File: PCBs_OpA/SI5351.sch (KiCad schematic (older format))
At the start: 12 parts, among them J4 CAL, Q1 2N7002, Q2 2N7002, U2 Si5351, Y1 25Mhz

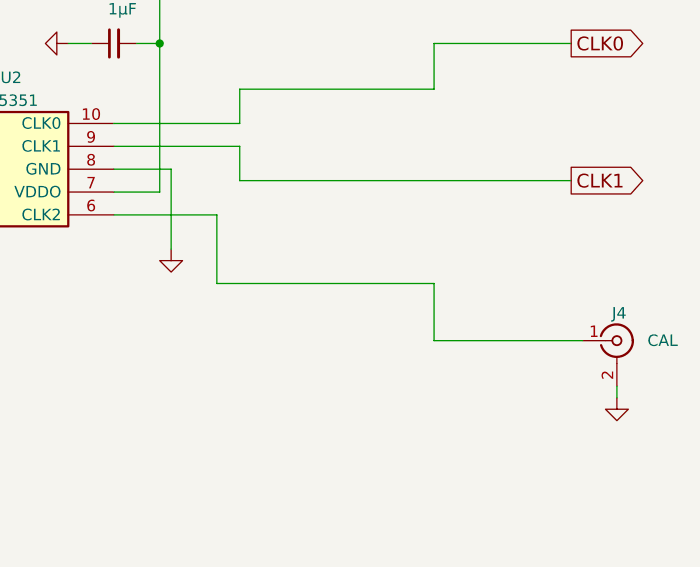
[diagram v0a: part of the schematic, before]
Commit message: add LPF/HPF RFSimm models
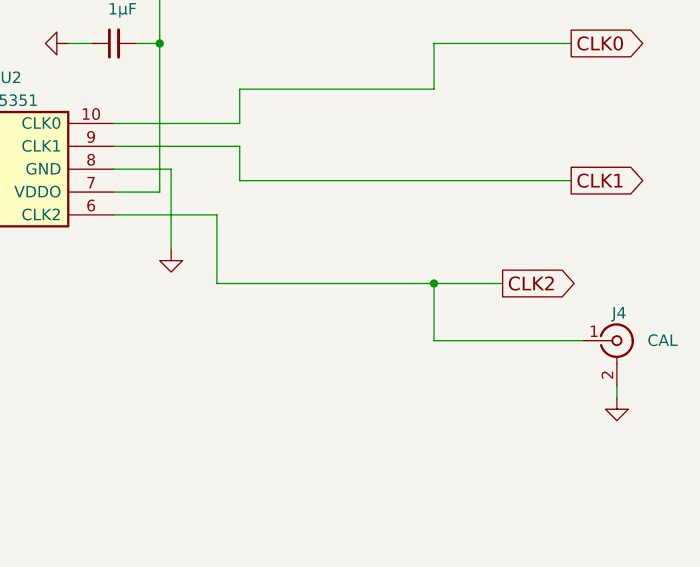
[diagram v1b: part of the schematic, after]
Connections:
- net CLK2: now reaches J4.1 (In), U2.6 (CLK2)
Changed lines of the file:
@@
 	6450 3450 6450 3750
 Wire Wire Line
-	6450 3750 7400 3750
+	6450 3750 7700 3750
 Wire Wire Line
 	6550 3300 8000 3300
@@
 Wire Wire Line
 	8200 4250 8200 4200
+Text GLabel 7700 3750 2    60   Output ~ 0
+CLK2
+Connection ~ 7400 3750
 $EndSCHEMATC

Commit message: Arduino Nano PCB ADX988 DSP
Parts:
- removed Q1, Q2: 2N7002, TO_SOT_Packages_SMD:SOT-23, symbol 2N7002
- removed R1, R3: 10K, LCSDR:R_1206_0603, symbol R_Small
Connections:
- net SCL: now also R4.2, U2.4 (SCL)
- net SDA: now also R11.2, U2.5 (SDA)
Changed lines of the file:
@@
 LIBS:BF998
 LIBS:relays
+LIBS:MCU_Microchip_ATtiny
 LIBS:LCSDR-cache
 EELAYER 25 0
@@
 Comment4 ""
 $EndDescr
-$Comp
-L 2N7002 Q2
-U 1 1 62501FAF
-P 3700 3250
-F 0 "Q2" V 3400 3500 50  0000 L CNN
-F 1 "2N7002" V 3550 3400 50  0000 L CNN
-F 2 "TO_SOT_Packages_SMD:SOT-23" H 3900 3175 50  0001 L CIN
-F 3 "" H 3700 3250 50  0001 L CNN
-	1    3700 3250
-	0    -1   1    0
-$EndComp
-$Comp
-L 2N7002 Q1
-U 1 1 62501FB6
-P 3600 4950
-F 0 "Q1" V 3350 5250 50  0000 L CNN
-F 1 "2N7002" V 3450 5050 50  0000 L CNN
-F 2 "TO_SOT_Packages_SMD:SOT-23" H 3800 4875 50  0001 L CIN
-F 3 "" H 3600 4950 50  0001 L CNN
-	1    3600 4950
-	0    -1   1    0
-$EndComp
-Text GLabel 2900 5050 0    60   BiDi ~ 0
+Text GLabel 3900 5050 0    60   BiDi ~ 0
 SDA
-Text GLabel 2850 3350 0    60   Output ~ 0
+Text GLabel 3900 3350 0    60   Output ~ 0
 SCL
-$Comp
-L +3.3V #PWR04
-U 1 1 62501FC5
-P 3600 4550
-F 0 "#PWR04" H 3600 4400 50  0001 C CNN
-F 1 "+3.3V" H 3600 4690 50  0000 C CNN
-F 2 "" H 3600 4550 50  0001 C CNN
-F 3 "" H 3600 4550 50  0001 C CNN
-	1    3600 4550
-	1    0    0    -1
-$EndComp
 $Comp
 L Si5351 U2
@@
 $EndComp
 $Comp
-L +3.3V #PWR05
+L +3.3V #PWR04
 U 1 1 62501FD9
 P 5000 2500
-F 0 "#PWR05" H 5000 2350 50  0001 C CNN
+F 0 "#PWR04" H 5000 2350 50  0001 C CNN
 F 1 "+3.3V" H 5000 2640 50  0000 C CNN
 F 2 "" H 5000 2500 50  0001 C CNN
@@
 $EndComp
 $Comp
-L GND #PWR06
+L GND #PWR05
 U 1 1 62501FDF
 P 6250 3600
-F 0 "#PWR06" H 6250 3350 50  0001 C CNN
+F 0 "#PWR05" H 6250 3350 50  0001 C CNN
 F 1 "GND" H 6250 3450 50  0001 C CNN
 F 2 "" H 6250 3600 50  0001 C CNN
@@
 $EndComp
 $Comp
-L +3.3V #PWR07
+L +3.3V #PWR06
 U 1 1 62501FE5
 P 6200 2100
-F 0 "#PWR07" H 6200 1950 50  0001 C CNN
+F 0 "#PWR06" H 6200 1950 50  0001 C CNN
 F 1 "+3.3V" H 6200 2240 50  0000 C CNN
 F 2 "" H 6200 2100 50  0001 C CNN
@@
 $EndComp
 $Comp
-L GND #PWR08
+L GND #PWR07
 U 1 1 6250203B
 P 5400 2700
-F 0 "#PWR08" H 5400 2450 50  0001 C CNN
+F 0 "#PWR07" H 5400 2450 50  0001 C CNN
 F 1 "GND" H 5400 2550 50  0001 C CNN
 F 2 "" H 5400 2700 50  0001 C CNN
@@
 $EndComp
 Wire Wire Line
-	2850 3350 3500 3350
-Wire Wire Line
-	2900 5050 3400 5050
-Wire Wire Line
-	3800 5050 4300 5050
+	3900 5050 4300 5050
 Wire Wire Line
 	4800 2750 4900 2750
@@
 Connection ~ 5000 2700
 Wire Wire Line
-	3600 4550 3600 4750
-Wire Wire Line
 	4000 2450 4000 3350
 Connection ~ 4000 3350
@@
 	4300 5050 4300 3450
 $Comp
-L +3.3V #PWR09
-U 1 1 62502072
-P 3700 2950
-F 0 "#PWR09" H 3700 2800 50  0001 C CNN
-F 1 "+3.3V" H 3700 3090 50  0000 C CNN
-F 2 "" H 3700 2950 50  0001 C CNN
-F 3 "" H 3700 2950 50  0001 C CNN
-	1    3700 2950
-	1    0    0    -1
-$EndComp
-Wire Wire Line
-	3700 2950 3700 3050
-$Comp
-L +3.3V #PWR010
+L +3.3V #PWR08
 U 1 1 6250207D
 P 4000 4000
-F 0 "#PWR010" H 4000 3850 50  0001 C CNN
+F 0 "#PWR08" H 4000 3850 50  0001 C CNN
 F 1 "+3.3V" H 4000 4140 50  0000 C CNN
 F 2 "" H 4000 4000 50  0001 C CNN
@@
 	1    0    0    -1
 $EndComp
-Wire Wire Line
-	3050 2450 3050 3350
-Connection ~ 3050 3350
 Wire Wire Line
 	3900 3350 5100 3350
@@
 $EndComp
 $Comp
-L GND #PWR011
+L GND #PWR09
 U 1 1 6253D2ED
 P 5800 2700
-F 0 "#PWR011" H 5800 2450 50  0001 C CNN
+F 0 "#PWR09" H 5800 2450 50  0001 C CNN
 F 1 "GND" H 5800 2550 50  0001 C CNN
 F 2 "" H 5800 2700 50  0001 C CNN
@@
 Text GLabel 8000 2700 2    60   Output ~ 0
 CLK0
-$Comp
-L R_Small R1
-U 1 1 630BFED6
-P 3050 2350
-F 0 "R1" H 3100 2400 50  0000 L CNN
-F 1 "10K" H 3100 2300 50  0000 L CNN
-F 2 "LCSDR:R_1206_0603" H 3050 2350 50  0001 C CNN
-F 3 "" H 3050 2350 50  0001 C CNN
-	1    3050 2350
-	1    0    0    -1
-$EndComp
-$Comp
-L R_Small R3
-U 1 1 630C009D
-P 3050 4250
-F 0 "R3" H 3100 4300 50  0000 L CNN
-F 1 "10K" H 3100 4200 50  0000 L CNN
-F 2 "LCSDR:R_1206_0603" H 3050 4250 50  0001 C CNN
-F 3 "" H 3050 4250 50  0001 C CNN
-	1    3050 4250
-	1    0    0    -1
-$EndComp
-Wire Wire Line
-	3050 4350 3050 5050
-Connection ~ 3050 5050
-$Comp
-L +5V #PWR012
-U 1 1 630C0187
-P 3050 4050
-F 0 "#PWR012" H 3050 3900 50  0001 C CNN
-F 1 "+5V" H 3050 4190 50  0000 C CNN
-F 2 "" H 3050 4050 50  0001 C CNN
-F 3 "" H 3050 4050 50  0001 C CNN
-	1    3050 4050
-	1    0    0    -1
-$EndComp
-Wire Wire Line
-	3050 4050 3050 4150
-$Comp
-L +5V #PWR013
-U 1 1 630C021D
-P 3050 2150
-F 0 "#PWR013" H 3050 2000 50  0001 C CNN
-F 1 "+5V" H 3050 2290 50  0000 C CNN
-F 2 "" H 3050 2150 50  0001 C CNN
-F 3 "" H 3050 2150 50  0001 C CNN
-	1    3050 2150
-	1    0    0    -1
-$EndComp
-Wire Wire Line
-	3050 2150 3050 2250
 $Comp
 L R_Small R4
@@
 $EndComp
 $Comp
-L +3.3V #PWR014
+L +3.3V #PWR010
 U 1 1 630C0393
 P 4000 2150
-F 0 "#PWR014" H 4000 2000 50  0001 C CNN
+F 0 "#PWR010" H 4000 2000 50  0001 C CNN
 F 1 "+3.3V" H 4000 2290 50  0000 C CNN
 F 2 "" H 4000 2150 50  0001 C CNN
@@
 $EndComp
 $Comp
-L GND #PWR015
+L GND #PWR011
 U 1 1 630C6EEC
 P 8200 4250
-F 0 "#PWR015" H 8200 4000 50  0001 C CNN
+F 0 "#PWR011" H 8200 4000 50  0001 C CNN
 F 1 "GND" H 8200 4100 50  0001 C CNN
 F 2 "" H 8200 4250 50  0001 C CNN
